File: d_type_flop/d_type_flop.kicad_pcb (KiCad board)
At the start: 2 copper layers, 32 parts, among them M11 PMOS, M12 PMOS, M13 NMOS, M14 NMOS, M21 PMOS, M22 PMOS, M23 NMOS, M24 NMOS, M31 PMOS, M32 PMOS, M33 PMOS, M34 NMOS, M35 NMOS, M36 NMOS, M41 PMOS, M42 PMOS, M43 NMOS, M44 NMOS, M51 PMOS, M52 PMOS, M53 NMOS, M54 NMOS, M61 PMOS, M62 PMOS, M63 NMOS, M64 NMOS, T1 TEST_1P, T2 TEST_1P, T3 TEST_1P, T4 TEST_1P, T5 TEST_1P, T6 TEST_1P

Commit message: more layout
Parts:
- moved T6 75.5 mm to (123.3, 49.0), turned to 180 degrees
- moved T4 72.2 mm to (97.2, 51.1), turned to 180 degrees
- moved T5 69.9 mm to (123.3, 51.2), turned to 180 degrees
- moved T3 69.6 mm to (97.2, 48.9), turned to 180 degrees
- moved T2 57.5 mm to (104.5, 51.1)
- moved T1 56.1 mm to (104.5, 48.9)
- turned M24 to 0 degrees
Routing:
- net (no net): track 125.9 -> 0.00 mm
- net GNDREF: track 16.7 -> 49.2 mm, vias 2 -> 4
- net /3/A: track 28.7 -> 55.7 mm, vias 0 -> 4
- net CLK: track 14.7 -> 39.0 mm, vias 0 -> 2
- net /4/A: track 10.8 -> 29.4 mm, vias 0 -> 2
- net D: track 5.88 -> 19.2 mm, vias 2 -> 1
- net Net-(M23-Pad3): track 13.2 -> 3.66 mm, vias 2 -> 0
- net +3V3: track 80.6 -> 87.2 mm, vias 2 -> 0
- net /2/A: track 29.4 -> 35.8 mm
- net /1/A: track 30.0 -> 32.0 mm
- net Net-(M43-Pad3): track 2.83 -> 3.44 mm

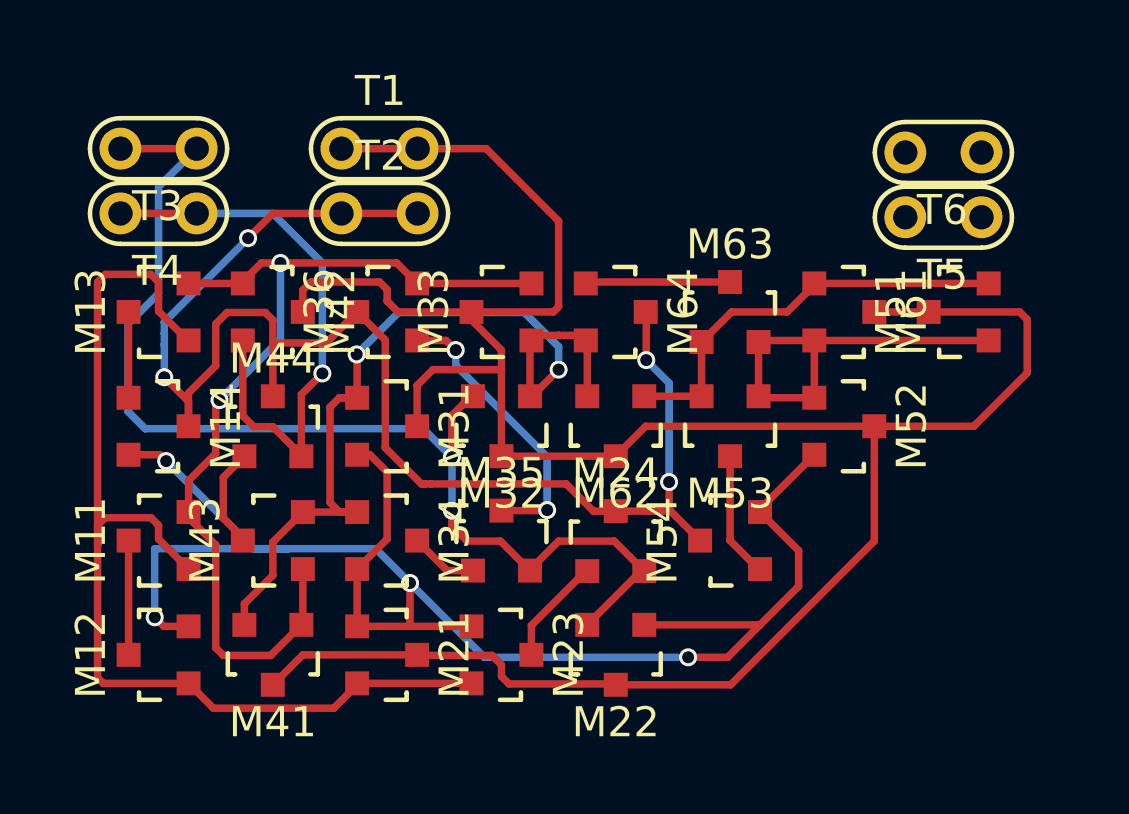
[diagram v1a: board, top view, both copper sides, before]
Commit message: Relayout headers and flood
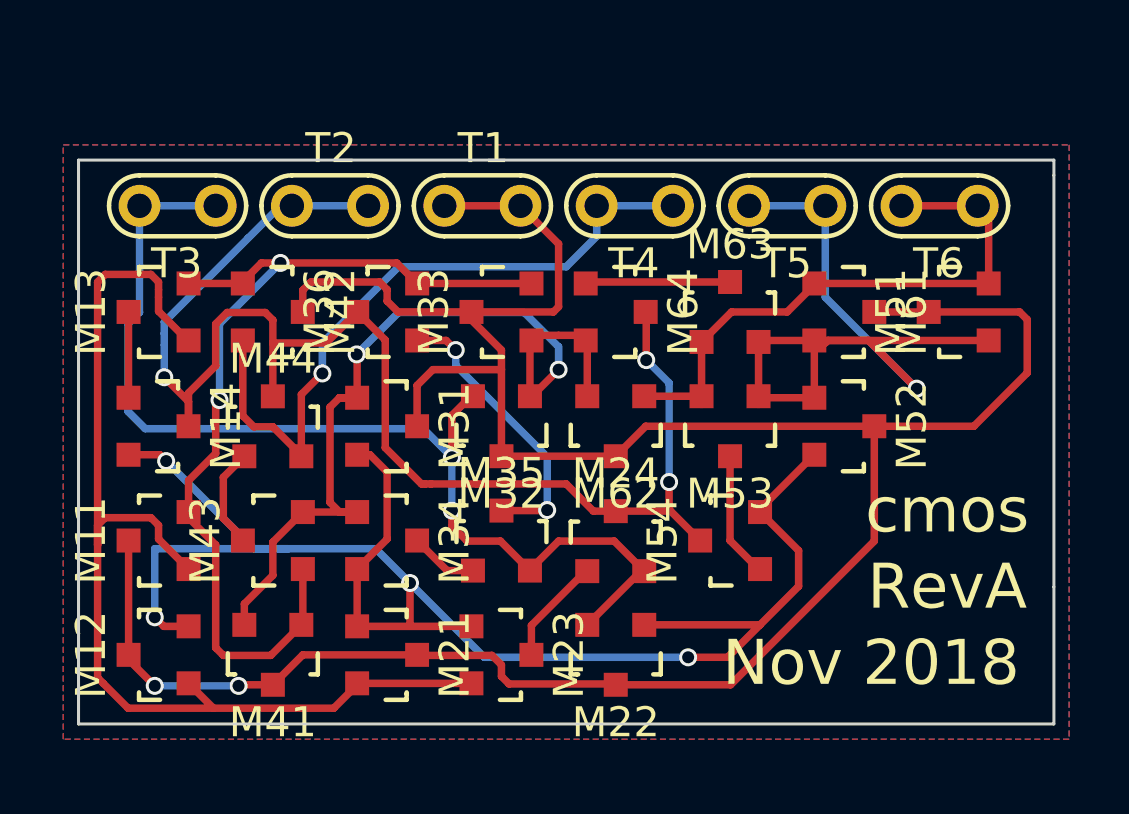
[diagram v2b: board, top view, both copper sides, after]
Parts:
- moved T4 15.9 mm to (113.0, 50.8)
- moved T5 5.22 mm to (118.1, 50.8)
- moved T1 3.92 mm to (108.0, 50.8)
- moved T3 2.01 mm to (97.8, 50.8)
- moved T6 1.78 mm to (123.2, 50.8)
- moved T2 1.67 mm to (102.9, 50.8)
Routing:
- net Q: track 13.3 -> 27.3 mm, vias 0 -> 1
- net nQ: track 14.1 -> 19.4 mm
- net D: track 19.2 -> 23.3 mm
- net CLK: track 39.0 -> 36.3 mm
- net GNDREF: track 49.2 -> 47.7 mm, vias 4 -> 3
- net /2/A: track 35.8 -> 37.0 mm
- net +3V3: track 87.2 -> 87.8 mm, vias 0 -> 2
- added copper zone on F.Cu, net +3V3
- added copper zone on B.Cu, net GNDREF
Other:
- board outline added: 32.5 x 18.8 mm
- rule trace_min: 0.2 -> 0
- board text added: "Nov 2018"
- board text added: "RevA"
- board text added: "cmos"

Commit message: P and N mark, thermal relief
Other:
- board text added: "- = NMOS"
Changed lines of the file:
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@@
     (links 73)
     (no_connects 0)
-    (area 93.88 45.7102 127.2 69.09322)
+    (area 93.88 47.6152 127.508001 69.09322)
     (thickness 1.6)
-    (drawings 9)
+    (drawings 24)
     (tracks 292)
     (zones 0)
@@
   (layers
     (0 F.Cu signal)
-    (31 B.Cu signal hide)
+    (31 B.Cu signal)
     (32 B.Adhes user)
     (33 F.Adhes user)
@@
     (mod_text_size 1 1)
     (mod_text_width 0.15)
-    (pad_size 1.5 1.5)
-    (pad_drill 0.6)
+    (pad_size 1.397 1.397)
+    (pad_drill 0.8128)
     (pad_to_mask_clearance 0)
     (aux_axis_origin 0 0)
@@
       (net 4 /3/A))
     (pad 3 smd rect (at 0 -0.99822 90) (size 0.8001 0.8001) (layers F.Cu F.Paste F.Mask)
-      (net 3 +3V3))
+      (net 3 +3V3) (zone_connect 2))
     (model TO_SOT_Packages_SMD.3dshapes/SOT-23.wrl
       (at (xyz 0 0 0))
@@
       (net 7 CLK))
     (pad 3 smd rect (at 0 -0.99822 180) (size 0.8001 0.8001) (layers F.Cu F.Paste F.Mask)
-      (net 3 +3V3))
+      (net 3 +3V3) (zone_connect 2))
     (model TO_SOT_Packages_SMD.3dshapes/SOT-23.wrl
       (at (xyz 0 0 0))
@@
       (net 2 /1/A))
     (pad 3 smd rect (at 0 -0.99822 90) (size 0.8001 0.8001) (layers F.Cu F.Paste F.Mask)
-      (net 3 +3V3))
+      (net 3 +3V3) (zone_connect 2))
     (model TO_SOT_Packages_SMD.3dshapes/SOT-23.wrl
       (at (xyz 0 0 0))
@@
       (net 9 /4/A))
     (pad 3 smd rect (at 0 -0.99822 180) (size 0.8001 0.8001) (layers F.Cu F.Paste F.Mask)
-      (net 3 +3V3))
+      (net 3 +3V3) (zone_connect 2))
     (model TO_SOT_Packages_SMD.3dshapes/SOT-23.wrl
       (at (xyz 0 0 0))
@@
       (net 4 /3/A))
     (pad 3 smd rect (at 0 -0.99822 270) (size 0.8001 0.8001) (layers F.Cu F.Paste F.Mask)
-      (net 3 +3V3))
+      (net 3 +3V3) (zone_connect 2))
     (model TO_SOT_Packages_SMD.3dshapes/SOT-23.wrl
       (at (xyz 0 0 0))
@@
       (net 9 /4/A))
     (pad 3 smd rect (at 0 -0.99822 180) (size 0.8001 0.8001) (layers F.Cu F.Paste F.Mask)
-      (net 3 +3V3))
+      (net 3 +3V3) (zone_connect 2))
     (model TO_SOT_Packages_SMD.3dshapes/SOT-23.wrl
       (at (xyz 0 0 0))
@@
     (fp_arc (start -1.27 0) (end -2.286 0) (angle 90) (layer F.SilkS) (width 0.15))
     (pad 1 thru_hole circle (at -1.27 0) (size 1.397 1.397) (drill 0.8128) (layers *.Cu *.Mask F.SilkS)
-      (net 3 +3V3))
+      (net 3 +3V3) (zone_connect 2))
     (pad 1 thru_hole circle (at 1.27 0) (size 1.397 1.397) (drill 0.8128) (layers *.Cu *.Mask F.SilkS)
-      (net 3 +3V3))
+      (net 3 +3V3) (zone_connect 2))
     (model Measurement_Points.3dshapes/Test_Point.wrl
       (at (xyz 0 0 0))
@@
     (fp_arc (start -1.27 0) (end -2.286 0) (angle 90) (layer F.SilkS) (width 0.15))
     (pad 1 thru_hole circle (at -1.27 0) (size 1.397 1.397) (drill 0.8128) (layers *.Cu *.Mask F.SilkS)
-      (net 6 GNDREF))
+      (net 6 GNDREF) (zone_connect 2))
     (pad 1 thru_hole circle (at 1.27 0) (size 1.397 1.397) (drill 0.8128) (layers *.Cu *.Mask F.SilkS)
-      (net 6 GNDREF))
+      (net 6 GNDREF) (zone_connect 2))
     (model Measurement_Points.3dshapes/Test_Point.wrl
       (at (xyz 0 0 0))
@@
     )
   )
+  (gr_text "- = NMOS" (at 119.253 63.627) (layer B.SilkS)
+    (effects (font (size 1.5 1.5) (thickness 0.3)) (justify mirror))
+  )
+  (gr_line (start 99.822 58.166) (end 101.981 58.166) (angle 90) (layer F.SilkS) (width 0.2))
+  (gr_line (start 108.585 64.643) (end 108.585 66.675) (angle 90) (layer F.SilkS) (width 0.2))
+  (gr_line (start 116.078 60.96) (end 116.078 62.865) (angle 90) (layer F.SilkS) (width 0.2))
+  (gr_line (start 113.411 62.103) (end 113.411 61.976) (angle 90) (layer F.SilkS) (width 0.2))
+  (gr_line (start 111.252 62.103) (end 113.411 62.103) (angle 90) (layer F.SilkS) (width 0.2))
+  (gr_line (start 107.569 61.976) (end 109.601 61.976) (angle 90) (layer F.SilkS) (width 0.2))
+  (gr_line (start 104.775 60.96) (end 104.775 62.865) (angle 90) (layer F.SilkS) (width 0.2))
+  (gr_line (start 100.838 60.96) (end 100.838 62.865) (angle 90) (layer F.SilkS) (width 0.2))
+  (gr_line (start 97.155 57.15) (end 97.155 59.182) (angle 90) (layer F.SilkS) (width 0.2))
+  (gr_line (start 115.062 58.166) (end 117.221 58.166) (angle 90) (layer F.SilkS) (width 0.2))
+  (gr_line (start 115.316 54.356) (end 117.348 54.356) (angle 90) (layer F.SilkS) (width 0.2))
+  (gr_line (start 112.268 53.34) (end 112.268 55.372) (angle 90) (layer F.SilkS) (width 0.2))
+  (gr_line (start 104.648 53.34) (end 104.648 55.372) (angle 90) (layer F.SilkS) (width 0.2))
+  (gr_line (start 97.028 53.34) (end 97.028 55.372) (angle 90) (layer F.SilkS) (width 0.2))
   (gr_text "Nov 2018" (at 120.904 66.04) (layer F.SilkS)
     (effects (font (size 1.5 1.5) (thickness 0.3)))

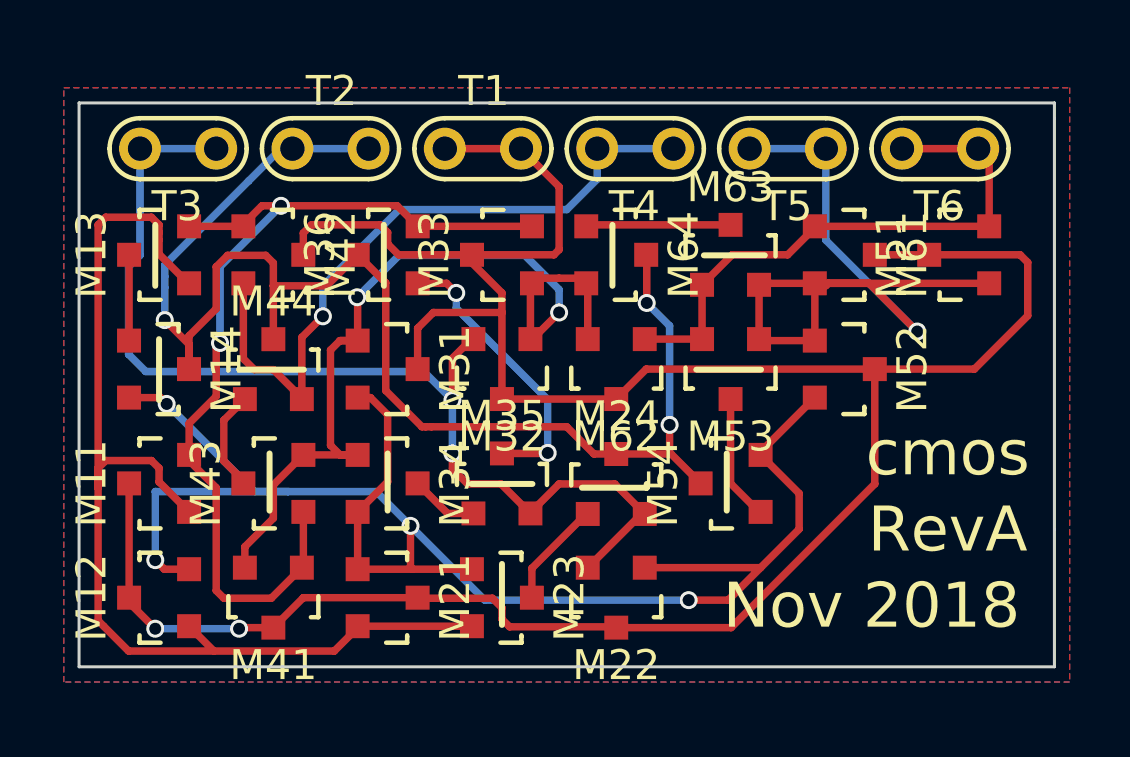
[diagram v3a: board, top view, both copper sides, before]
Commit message: Export gerbers and adjust floods
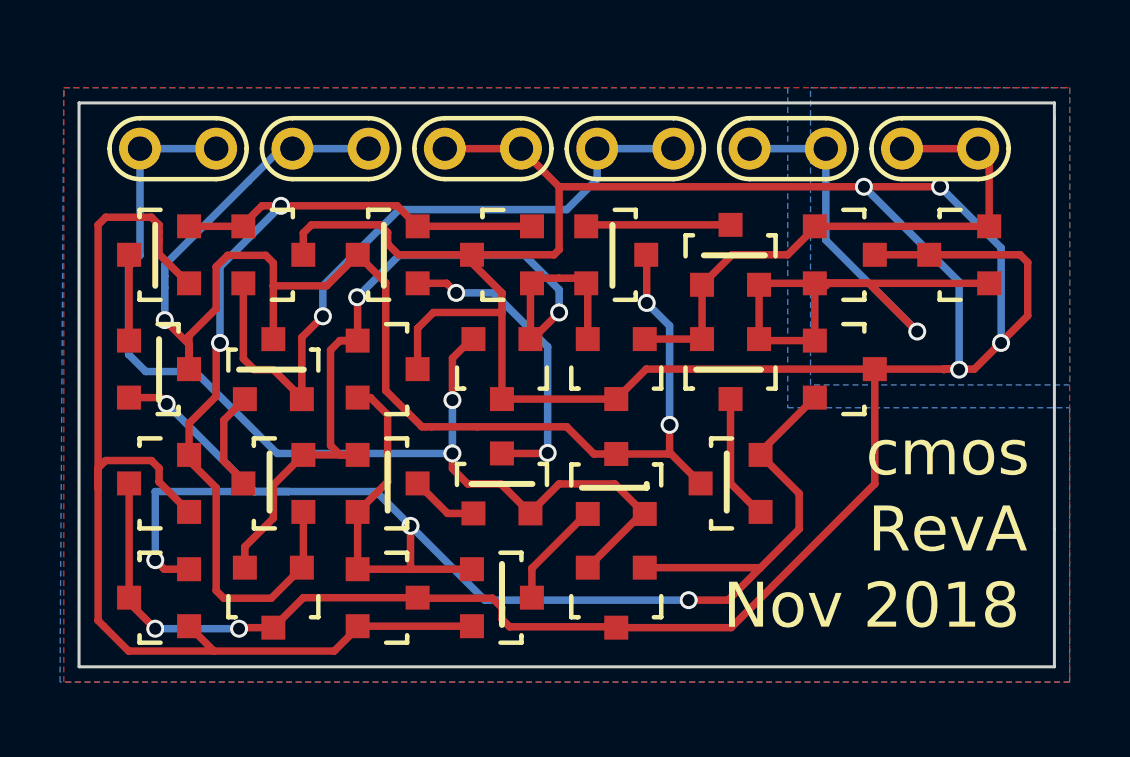
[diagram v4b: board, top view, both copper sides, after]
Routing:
- net +3V3: track 87.8 -> 114.8 mm, vias 2 -> 6
- net Net-(M35-Pad3): track 9.55 -> 10.3 mm
- net CLK: track 36.3 -> 37.0 mm
- added copper zone on B.Cu, net +3V3
